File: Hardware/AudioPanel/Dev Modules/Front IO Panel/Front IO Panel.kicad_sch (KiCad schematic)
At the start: 79 parts, among them J101 2.54mm, J102 JST-PH UART/I2C, J103 2.54mm, J104 Screw_Terminal_01x02, U101 NXB0106BQX, U102 QTPy SAMD21, U103 USBLC6-2SC6, U104 USBLC6-2SC6, U105 AZ1117-5.0, U106 AP3012, U107 INA219AxDCN

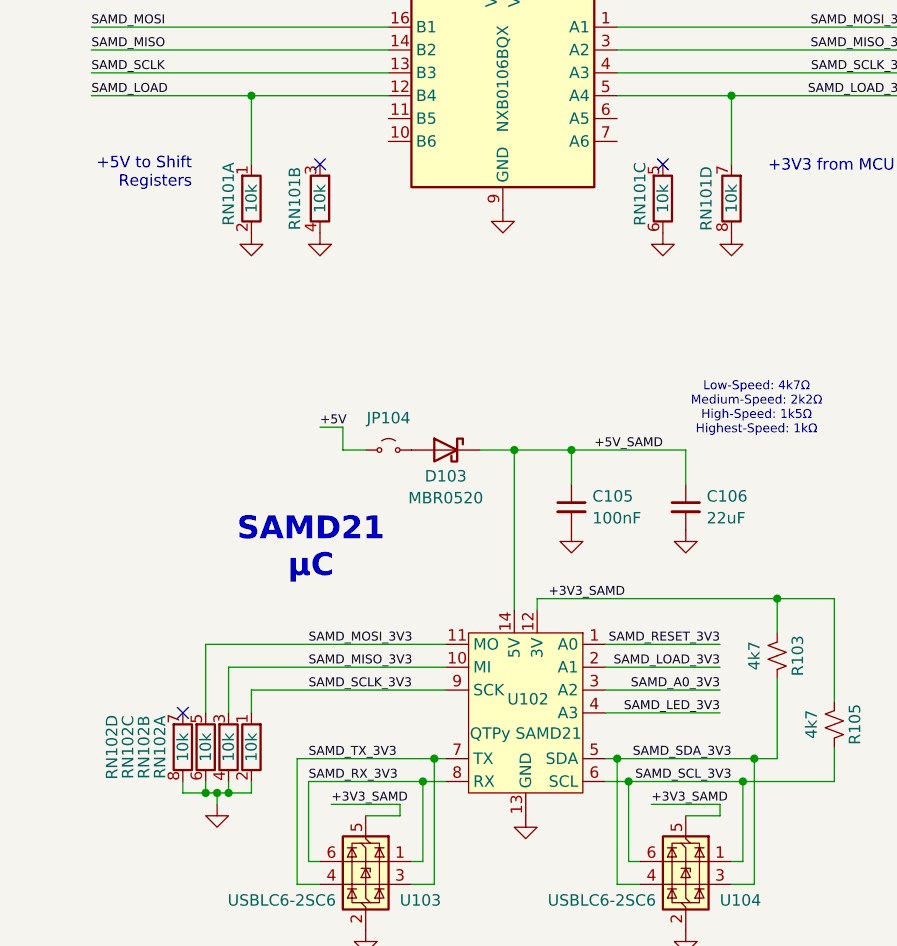
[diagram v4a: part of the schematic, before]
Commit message: Changed LED and Resistor Array packages
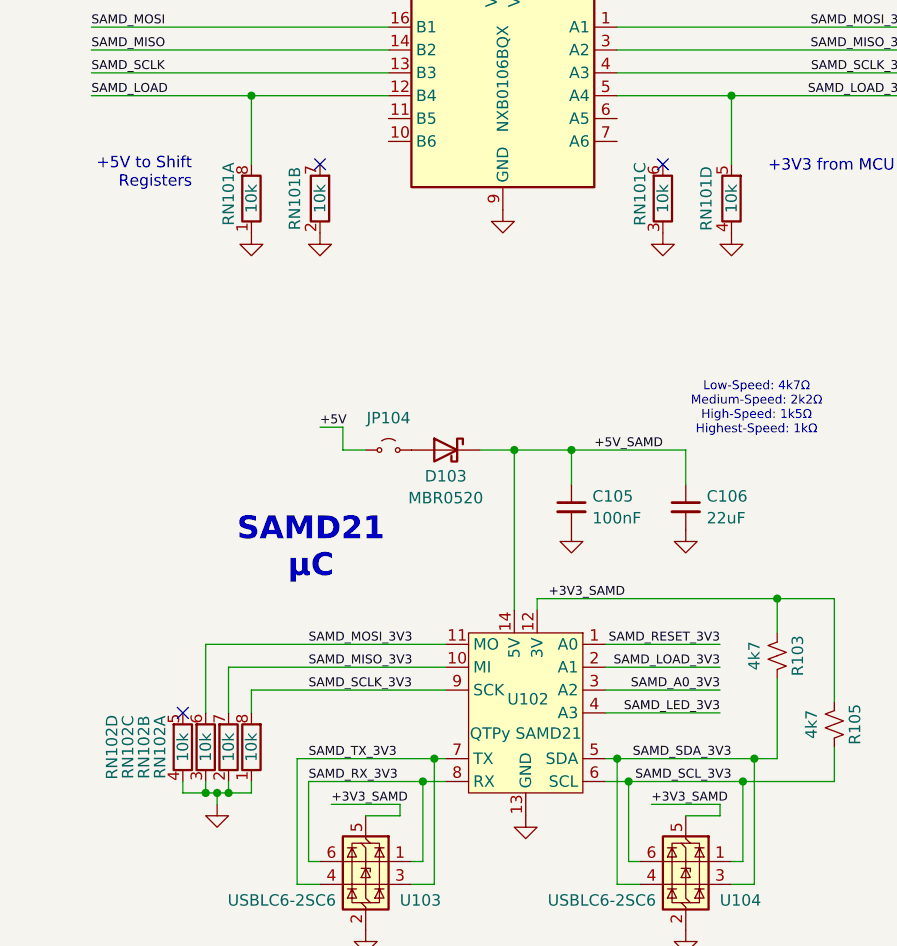
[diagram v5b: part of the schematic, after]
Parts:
- D101, D102, D105: footprint LED_THT:LED_D5.0mm -> Libraries:Worthington_LED_0603
- R101, R102, R106, R111, R112: footprint Libraries:Worthington_R_0603 -> Libraries:Worthington_R_0402
- R103, R105: footprint Resistor_SMD:R_0402_1005Metric -> Libraries:Worthington_R_0402
- R108: footprint Capacitor_SMD:C_1206_3216Metric -> Libraries:Worthington_R_0402
- RN101, RN102: footprint Resistor_SMD:R_Array_Convex_4x1206 -> Libraries:RES_ARRAY_4RES_0804; symbol Library_MicSwitcher:R_Network04_Split -> Libraries:R_Network04_Split
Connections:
- net GND: now also RN101.1 (4), RN101.2, RN101.3, RN101.4, RN102.1 (4), RN102.2, RN102.3, RN102.4; no longer RN101.2, RN101.4, RN101.6, RN101.8, RN102.2, RN102.4, RN102.6, RN102.8
- net SAMD_LOAD: now also RN101.8; no longer RN101.1
- net SAMD_LOAD_3V3: now also RN101.5; no longer RN101.7
- net SAMD_MISO_3V3: now also RN102.7 (5); no longer RN102.3
- net SAMD_MOSI_3V3: now also RN102.6; no longer RN102.5
- net SAMD_SCLK_3V3: now also RN102.8; no longer RN102.1
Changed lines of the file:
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@@
 			)
 		)
-		(property "Footprint" "LED_THT:LED_D5.0mm"
+		(property "Footprint" "Libraries:Worthington_LED_0603"
 			(at 40.64 167.64 0)
 			(effects
@@
 	)
 	(symbol
-		(lib_id "Library_MicSwitcher:R_Network04_Split")
+		(lib_id "Libraries:R_Network04_Split")
 		(at 264.16 107.95 0)
 		(unit 4)
@@
 			)
 		)
-		(property "Footprint" "Resistor_SMD:R_Array_Convex_4x1206"
+		(property "Footprint" "Libraries:RES_ARRAY_4RES_0804"
 			(at 262.128 107.95 90)
 			(effects
@@
 			)
 		)
-		(property "Footprint" "Libraries:Worthington_R_0603"
+		(property "Footprint" "Libraries:Worthington_R_0402"
 			(at 40.64 176.53 0)
 			(effects
@@
 			)
 		)
-		(property "Footprint" "Resistor_SMD:R_0402_1005Metric"
+		(property "Footprint" "Libraries:Worthington_R_0402"
 			(at 269.24 158.75 0)
 			(effects
@@
 	)
 	(symbol
-		(lib_id "Library_MicSwitcher:R_Network04_Split")
+		(lib_id "Libraries:R_Network04_Split")
 		(at 210.82 168.91 0)
 		(unit 1)
@@
 			)
 		)
-		(property "Footprint" "Resistor_SMD:R_Array_Convex_4x1206"
+		(property "Footprint" "Libraries:RES_ARRAY_4RES_0804"
 			(at 208.788 168.91 90)
 			(effects
@@
 			)
 		)
-		(property "Footprint" "Capacitor_SMD:C_1206_3216Metric"
+		(property "Footprint" "Libraries:Worthington_R_0402"
 			(at 260.35 232.41 0)
 			(effects
@@
 			)
 		)
-		(property "Footprint" "LED_THT:LED_D5.0mm"
+		(property "Footprint" "Libraries:Worthington_LED_0603"
 			(at 40.64 111.76 0)
 			(effects
@@
 	)
 	(symbol
-		(lib_id "Library_MicSwitcher:R_Network04_Split")
+		(lib_id "Libraries:R_Network04_Split")
 		(at 210.82 107.95 0)
 		(mirror y)
@@
 			)
 		)
-		(property "Footprint" "Resistor_SMD:R_Array_Convex_4x1206"
+		(property "Footprint" "Libraries:RES_ARRAY_4RES_0804"
 			(at 212.852 107.95 90)
 			(effects
@@
 	)
 	(symbol
-		(lib_id "Library_MicSwitcher:R_Network04_Split")
+		(lib_id "Libraries:R_Network04_Split")
 		(at 218.44 107.95 0)
 		(unit 2)
@@
 			)
 		)
-		(property "Footprint" "Resistor_SMD:R_Array_Convex_4x1206"
+		(property "Footprint" "Libraries:RES_ARRAY_4RES_0804"
 			(at 216.408 107.95 90)
 			(effects
@@
 	)
 	(symbol
-		(lib_id "Library_MicSwitcher:R_Network04_Split")
+		(lib_id "Libraries:R_Network04_Split")
 		(at 256.54 107.95 0)
 		(mirror y)
@@
 			)
 		)
-		(property "Footprint" "Resistor_SMD:R_Array_Convex_4x1206"
+		(property "Footprint" "Libraries:RES_ARRAY_4RES_0804"
 			(at 258.572 107.95 90)
 			(effects
@@
 			)
 		)
-		(property "Footprint" "Libraries:Worthington_R_0603"
+		(property "Footprint" "Libraries:Worthington_R_0402"
 			(at 40.64 74.93 0)
 			(effects
@@
 			)
 		)
-		(property "Footprint" "Libraries:Worthington_R_0603"
+		(property "Footprint" "Libraries:Worthington_R_0402"
 			(at 289.56 247.65 0)
 			(effects
@@
 	)
 	(symbol
-		(lib_id "Library_MicSwitcher:R_Network04_Split")
+		(lib_id "Libraries:R_Network04_Split")
 		(at 208.28 168.91 0)
 		(mirror y)
@@
 			)
 		)
-		(property "Footprint" "Resistor_SMD:R_Array_Convex_4x1206"
+		(property "Footprint" "Libraries:RES_ARRAY_4RES_0804"
 			(at 210.312 168.91 90)
 			(effects
@@
 			)
 		)
-		(property "Footprint" "Resistor_SMD:R_0402_1005Metric"
+		(property "Footprint" "Libraries:Worthington_R_0402"
 			(at 275.59 166.37 0)
 			(effects
@@
 			)
 		)
-		(property "Footprint" "Libraries:Worthington_R_0603"
+		(property "Footprint" "Libraries:Worthington_R_0402"
 			(at 40.64 120.65 0)
 			(effects
@@
 			)
 		)
-		(property "Footprint" "Libraries:Worthington_R_0603"
+		(property "Footprint" "Libraries:Worthington_R_0402"
 			(at 133.35 242.57 0)
 			(effects
@@
 	)
 	(symbol
-		(lib_id "Library_MicSwitcher:R_Network04_Split")
+		(lib_id "Libraries:R_Network04_Split")
 		(at 205.74 168.91 0)
 		(mirror y)
@@
 			)
 		)
-		(property "Footprint" "Resistor_SMD:R_Array_Convex_4x1206"
+		(property "Footprint" "Libraries:RES_ARRAY_4RES_0804"
 			(at 207.772 168.91 90)
 			(effects
@@
 	)
 	(symbol
-		(lib_id "Library_MicSwitcher:R_Network04_Split")
+		(lib_id "Libraries:R_Network04_Split")
 		(at 203.2 168.91 0)
 		(mirror y)
@@
 			)
 		)
-		(property "Footprint" "Resistor_SMD:R_Array_Convex_4x1206"
+		(property "Footprint" "Libraries:RES_ARRAY_4RES_0804"
 			(at 205.232 168.91 90)
 			(effects
@@
 			)
 		)
-		(property "Footprint" "LED_THT:LED_D5.0mm"
+		(property "Footprint" "Libraries:Worthington_LED_0603"
 			(at 40.64 66.04 0)
 			(effects

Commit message: Changed SAMD21 to through-hole footprint
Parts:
- U102: footprint Libraries:Py_QT_SAMD21 -> Libraries:Py_QT_SAMD21_THT
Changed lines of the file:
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@@
 			)
 		)
-		(property "Footprint" "Libraries:Py_QT_SAMD21"
+		(property "Footprint" "Libraries:Py_QT_SAMD21_THT"
 			(at 250.19 157.48 0)
 			(effects
